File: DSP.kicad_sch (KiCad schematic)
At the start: 19 parts, among them J2 Conn_01x04, J4 Conn_01x04, J5 Conn_01x04, U4 STM32F103C6Tx, Y1 16MHz

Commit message: Added polygons
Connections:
- net V_USB is gone; now on net +3V3: J2.1 (Pin_1), J4.1 (Pin_1), J5.1 (Pin_1)
- net PB12 renamed RAM_nCS
- net PB13 renamed SD_nCS
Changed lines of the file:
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@@
-    )
-  )
-  (global_label "V_USB" (shape input) (at 214.63 97.79 90) (fields_autoplaced)
-    (effects (font (size 1 1)) (justify left))
-    (property "Intersheet References" "${INTERSHEET_REFS}" (id 0) (at 214.5675 91.271 90)
-      (effects (font (size 1 1)) (justify left) hide)
     )
   )
@@
     )
   )
-  (global_label "PB12" (shape input) (at 92.71 110.49 180) (fields_autoplaced)
-    (effects (font (size 1 1)) (justify right))
-    (property "Intersheet References" "${INTERSHEET_REFS}" (id 0) (at 86.9052 110.4275 0)
-      (effects (font (size 1 1)) (justify right) hide)
-    )
-  )
   (global_label "Tx" (shape input) (at 198.12 124.46 180) (fields_autoplaced)
     (effects (font (size 1 1)) (justify right))
@@
     )
   )
-  (global_label "PB13" (shape input) (at 92.71 113.03 180) (fields_autoplaced)
-    (effects (font (size 1 1)) (justify right))
-    (property "Intersheet References" "${INTERSHEET_REFS}" (id 0) (at 86.9052 112.9675 0)
+  (global_label "RAM_nCS" (shape input) (at 92.71 110.49 180) (fields_autoplaced)
+    (effects (font (size 1 1)) (justify right))
+    (property "Intersheet References" "${INTERSHEET_REFS}" (id 0) (at 84.191 110.5525 0)
       (effects (font (size 1 1)) (justify right) hide)
     )
@@
     )
   )
-  (global_label "V_USB" (shape input) (at 196.85 118.11 90) (fields_autoplaced)
-    (effects (font (size 1 1)) (justify left))
-    (property "Intersheet References" "${INTERSHEET_REFS}" (id 0) (at 196.7875 111.591 90)
-      (effects (font (size 1 1)) (justify left) hide)
-    )
-  )
   (global_label "PC15" (shape input) (at 92.71 74.93 180) (fields_autoplaced)
     (effects (font (size 1 1)) (justify right))
@@
     )
   )
-  (global_label "V_USB" (shape input) (at 186.69 97.79 90) (fields_autoplaced)
-    (effects (font (size 1 1)) (justify left))
-    (property "Intersheet References" "${INTERSHEET_REFS}" (id 0) (at 186.6275 91.271 90)
-      (effects (font (size 1 1)) (justify left) hide)
-    )
-  )
   (global_label "Tx" (shape input) (at 125.73 102.87 0) (fields_autoplaced)
     (effects (font (size 1 1)) (justify left))
@@
     (effects (font (size 1 1)) (justify right))
     (property "Intersheet References" "${INTERSHEET_REFS}" (id 0) (at 86.9052 115.5075 0)
+      (effects (font (size 1 1)) (justify right) hide)
+    )
+  )
+  (global_label "SD_nCS" (shape input) (at 92.71 113.03 180) (fields_autoplaced)
+    (effects (font (size 1 1)) (justify right))
+    (property "Intersheet References" "${INTERSHEET_REFS}" (id 0) (at 85.2386 112.9675 0)
       (effects (font (size 1 1)) (justify right) hide)
     )
@@
     (pin "1")
   )
+  (symbol (lib_id "power:+3.3V") (at 214.63 97.79 0) (unit 1)
+    (in_bom yes) (on_board yes) (fields_autoplaced)
+    (property "Reference" "#PWR?" (id 0) (at 214.63 101.6 0)
+      (effects (font (size 1.27 1.27)) hide)
+    )
+    (property "Value" "+3.3V" (id 1) (at 214.63 92.71 0))
+    (property "Footprint" "" (id 2) (at 214.63 97.79 0)
+      (effects (font (size 1.27 1.27)) hide)
+    )
+    (property "Datasheet" "" (id 3) (at 214.63 97.79 0)
+      (effects (font (size 1.27 1.27)) hide)
+    )
+    (pin "1")
+  )
   (symbol (lib_id "Device:C_Small") (at 142.24 52.07 0) (unit 1)
     (in_bom yes) (on_board yes)
@@
     (pin "1")
     (pin "2")
+  )
+  (symbol (lib_id "power:+3.3V") (at 186.69 97.79 0) (unit 1)
+    (in_bom yes) (on_board yes) (fields_autoplaced)
+    (property "Reference" "#PWR?" (id 0) (at 186.69 101.6 0)
+      (effects (font (size 1.27 1.27)) hide)
+    )
+    (property "Value" "+3.3V" (id 1) (at 186.69 92.71 0))
+    (property "Footprint" "" (id 2) (at 186.69 97.79 0)
+      (effects (font (size 1.27 1.27)) hide)
+    )
+    (property "Datasheet" "" (id 3) (at 186.69 97.79 0)
+      (effects (font (size 1.27 1.27)) hide)
+    )
+    (pin "1")
   )
   (symbol (lib_id "power:GND") (at 86.36 172.72 0) (unit 1)
@@
     (pin "9")
   )
+  (symbol (lib_id "power:+3.3V") (at 196.85 118.11 0) (unit 1)
+    (in_bom yes) (on_board yes) (fields_autoplaced)
+    (property "Reference" "#PWR?" (id 0) (at 196.85 121.92 0)
+      (effects (font (size 1.27 1.27)) hide)
+    )
+    (property "Value" "+3.3V" (id 1) (at 196.85 113.03 0))
+    (property "Footprint" "" (id 2) (at 196.85 118.11 0)
+      (effects (font (size 1.27 1.27)) hide)
+    )
+    (property "Datasheet" "" (id 3) (at 196.85 118.11 0)
+      (effects (font (size 1.27 1.27)) hide)
+    )
+    (pin "1")
+  )
   (symbol (lib_id "power:GND") (at 78.74 143.51 0) (unit 1)

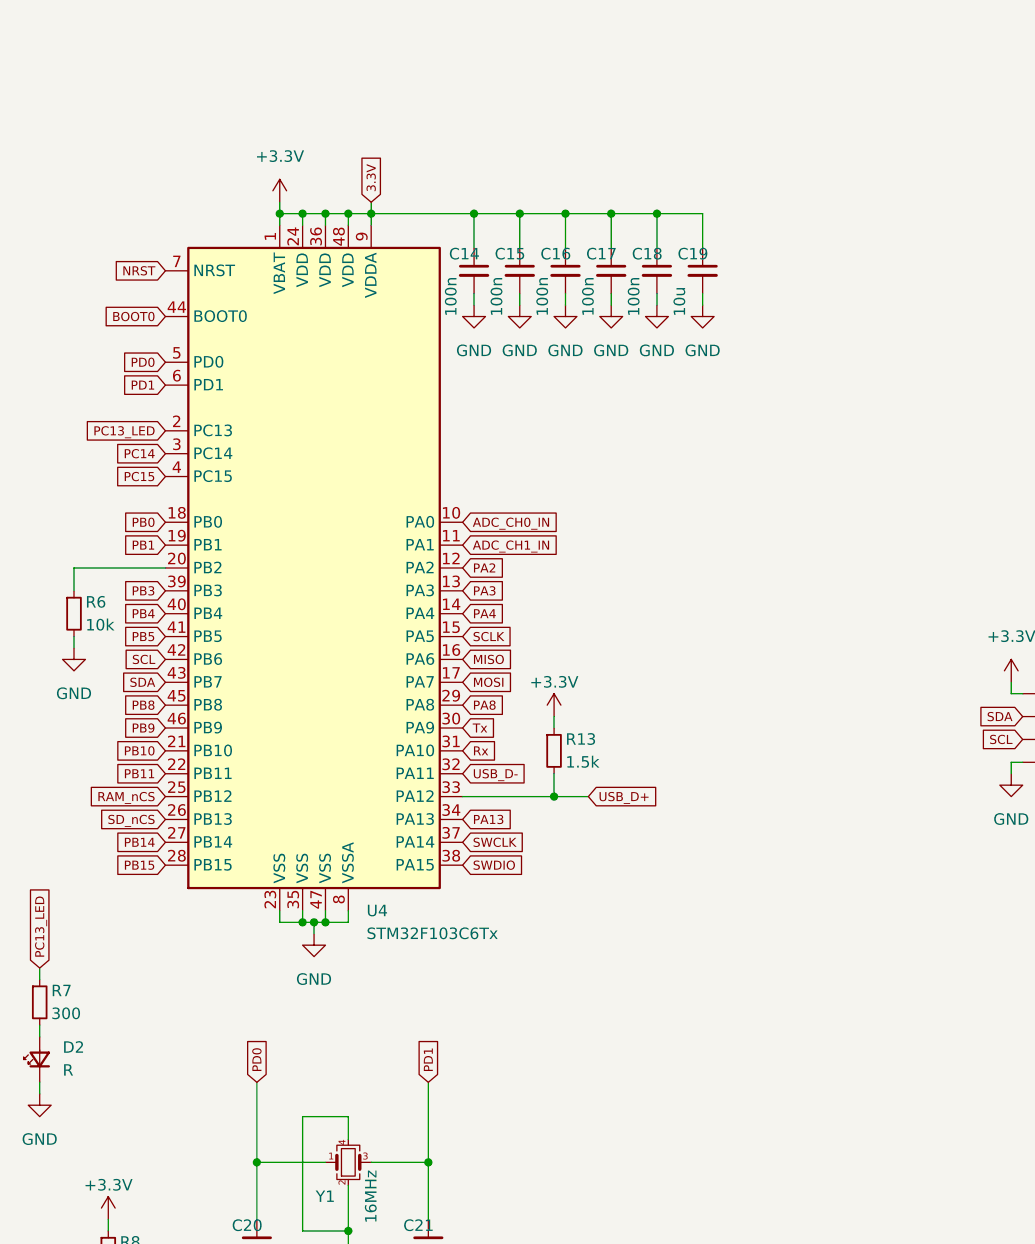
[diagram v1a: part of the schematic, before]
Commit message: had to change mcu since the stm32f103 does not have an FPU -> too slow for DSP applications
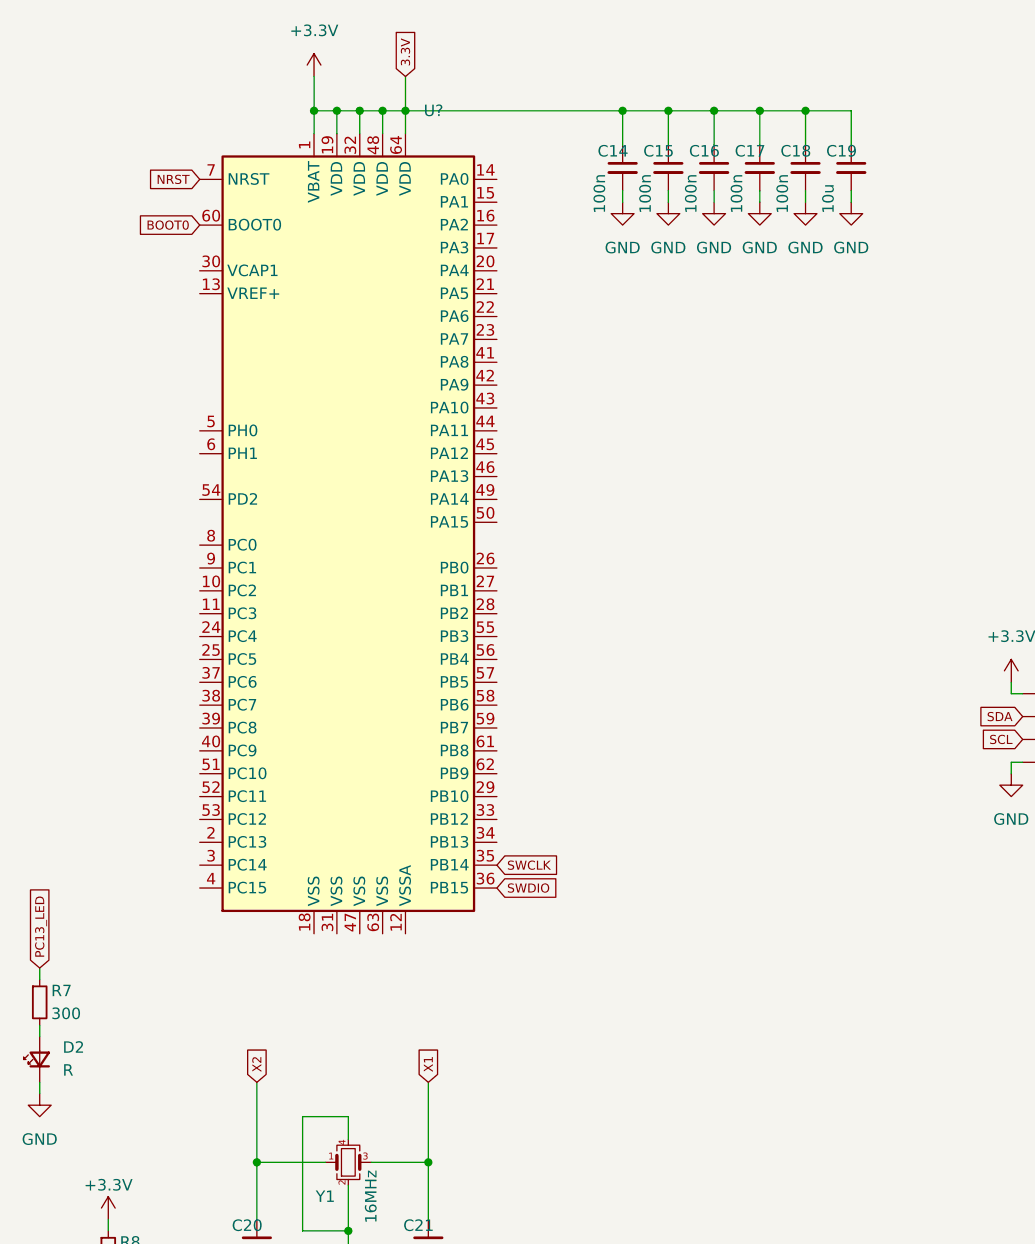
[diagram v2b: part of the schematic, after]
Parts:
- removed R13: 1.5k, Resistor_SMD:R_0603_1608Metric_Pad0.98x0.95mm_HandSolder, symbol Device:R_Small
- removed R6: 10k, Resistor_SMD:R_0603_1608Metric_Pad0.98x0.95mm_HandSolder, symbol Device:R_Small
- removed U4: STM32F103C6Tx, Package_QFP:LQFP-48_7x7mm_P0.5mm, symbol MCU_ST_STM32F1:STM32F103C6Tx
- added U?: (no value), symbol MCU_ST_STM32F4:STM32F401RBTx
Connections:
- net +3V3: now also U?.1 (VBAT), U?.19 (VDD), U?.32 (VDD), U?.48 (VDD), U?.64 (VDD)
- net BOOT0: now also U?.60 (BOOT0)
- net NRST: now also U?.7 (NRST)
- net SWCLK: now also U?.35 (PB14)
- net SWDIO: now also U?.36 (PB15)
- net PD0 renamed X2
- net PD1 renamed X1
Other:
- moved on the sheet: C14, C15, C16, C17, C18, C19

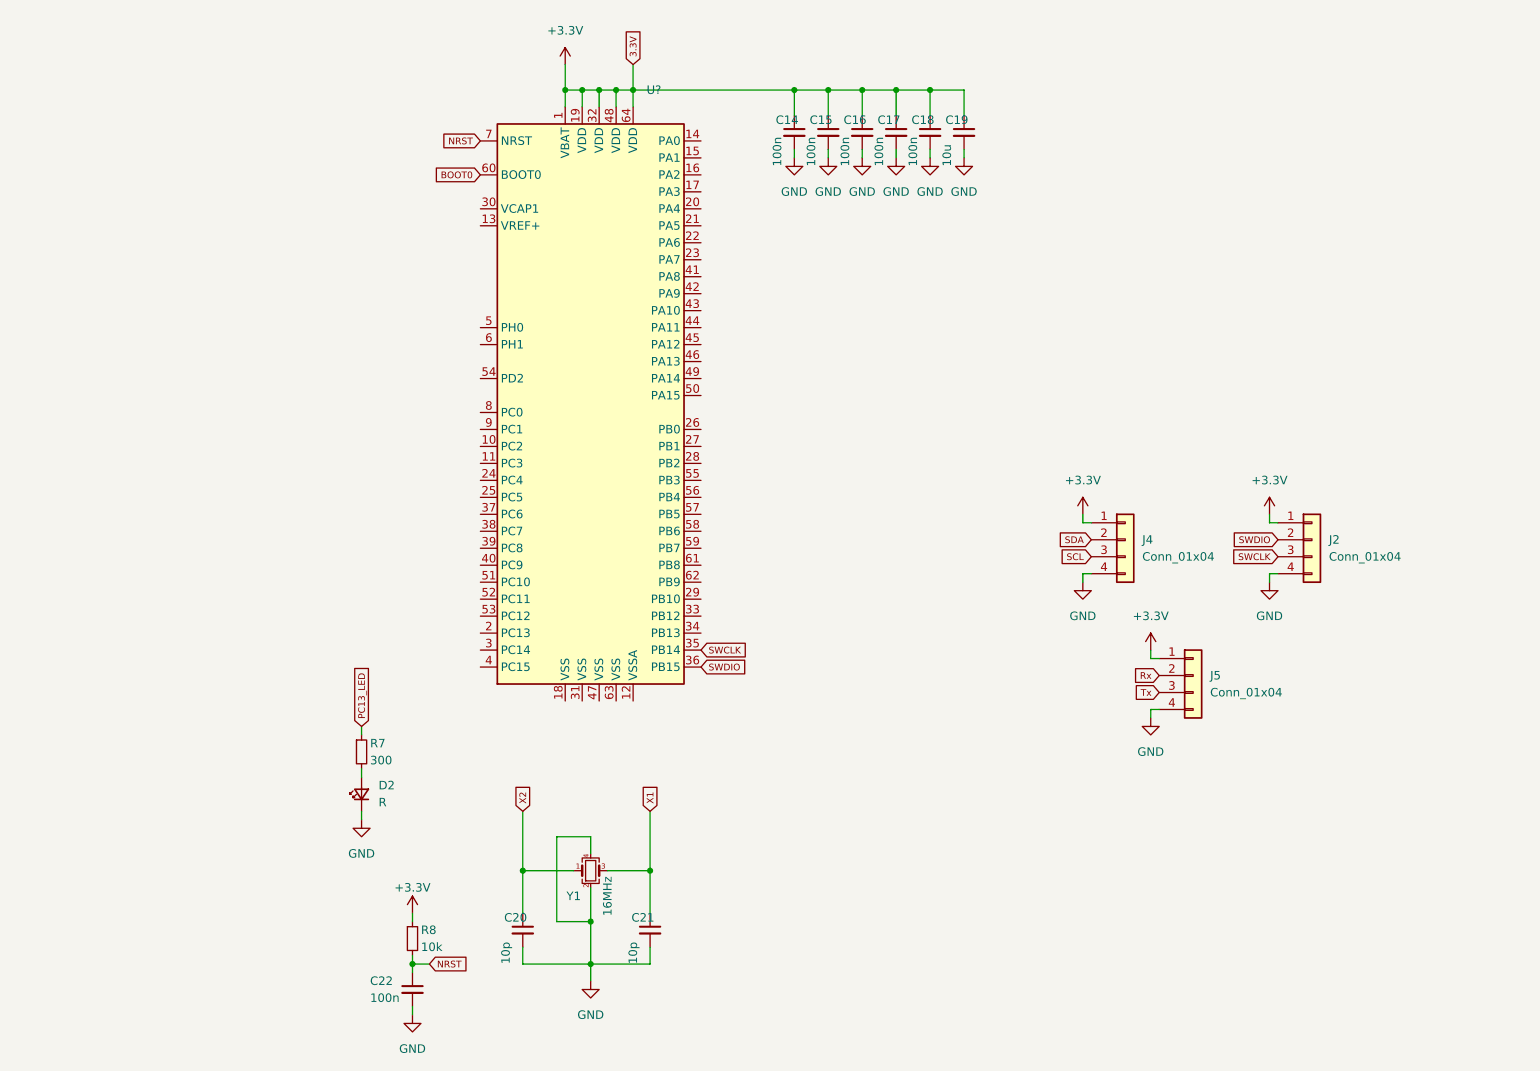
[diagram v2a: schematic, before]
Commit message: completed schematic and layout with new mcu, also added an SPI connector
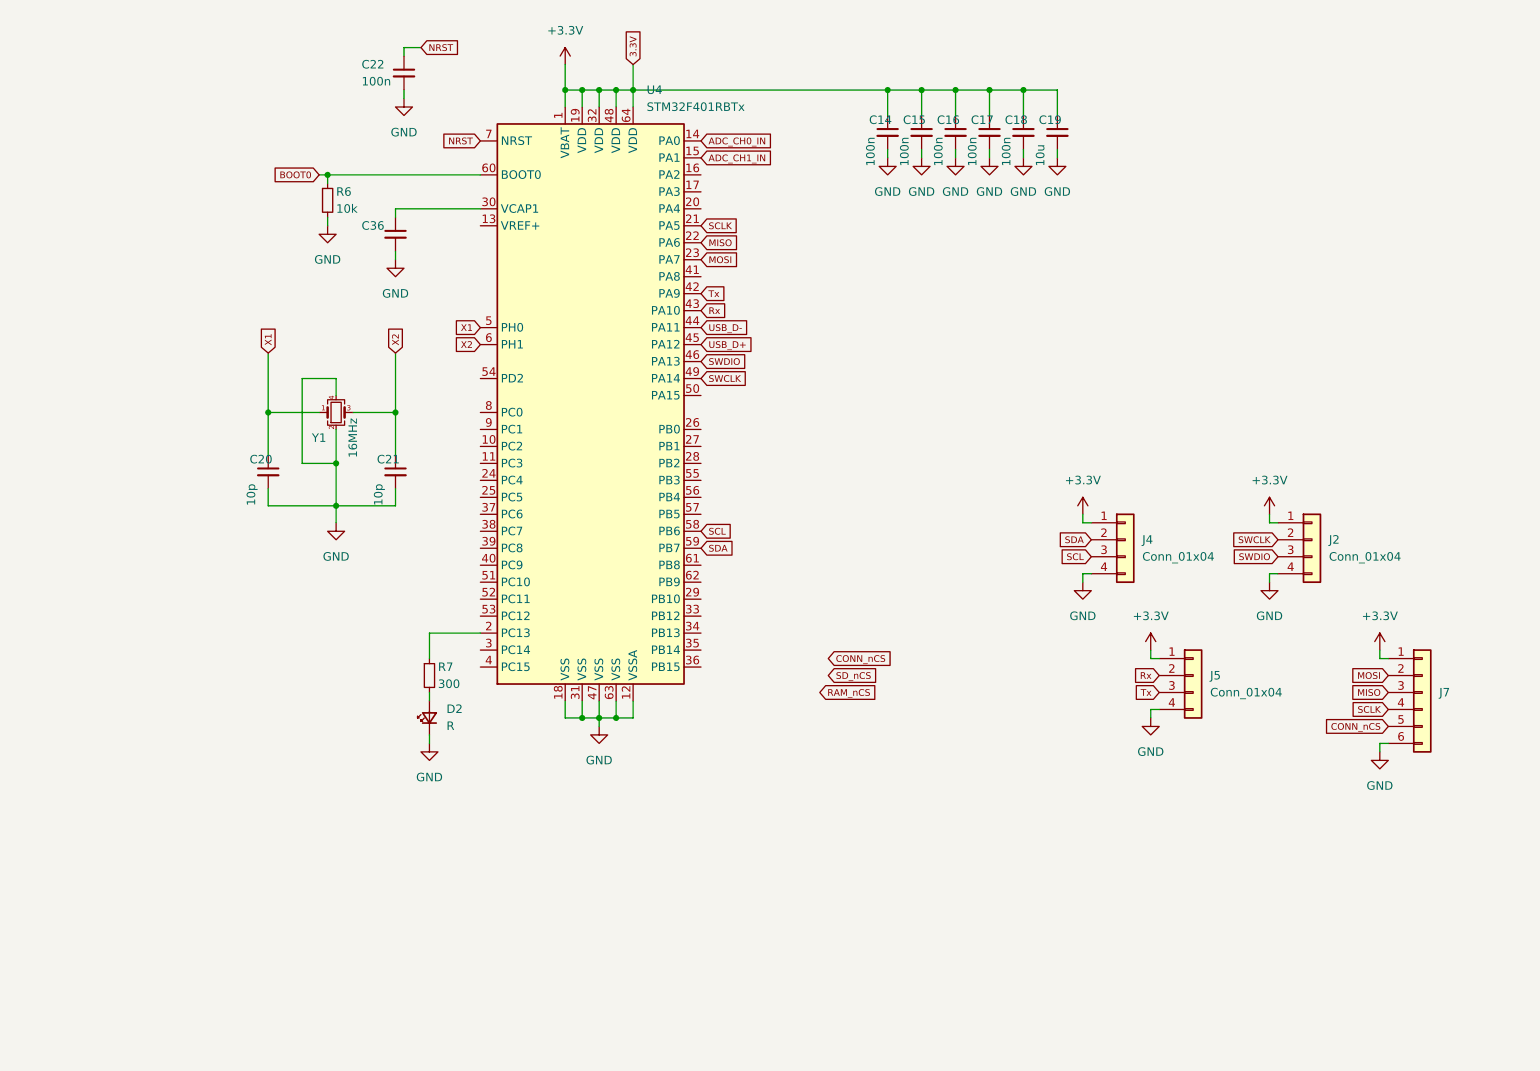
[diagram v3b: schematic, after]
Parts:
- removed R8: 10k, Resistor_SMD:R_0603_1608Metric_Pad0.98x0.95mm_HandSolder, symbol Device:R_Small
- added C36: (no value), symbol Device:C_Small
- added J7: (no value), symbol Connector_Generic:Conn_01x06
- added R6: 10k, Resistor_SMD:R_0603_1608Metric_Pad0.98x0.95mm_HandSolder, symbol Device:R_Small
- U4: renamed from U?; value (none) -> STM32F401RBTx; footprint (none) -> Package_QFP:LQFP-64_10x10mm_P0.5mm
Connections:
- net PC13_LED is gone; now on an unnamed net: R7.1
- net +3V3: now also J7.1 (Pin_1)
- net BOOT0: now also R6.1
- net GND: now also U4.12 (VSSA), U4.18 (VSS), U4.31 (VSS), U4.47 (VSS), U4.63 (VSS), C36.2, J7.6 (Pin_6), R6.2
- net Rx: now also U4.43 (PA10)
- net SCL: now also U4.58 (PB6)
- net SDA: now also U4.59 (PB7)
- net SWCLK: now also J2.2 (Pin_2), U4.49 (PA14); no longer J2.3 (Pin_3), U4.35 (PB14)
- net SWDIO: now also J2.3 (Pin_3), U4.46 (PA13); no longer J2.2 (Pin_2), U4.36 (PB15)
- net Tx: now also U4.42 (PA9)
- net X1: now also C20.1, U4.5 (PH0), Y1.1; no longer C21.1, Y1.3
- net X2: now also C21.1, U4.6 (PH1), Y1.3; no longer C20.1, Y1.1
- net ADC_CH0_IN: now reaches U4.14 (PA0)
- net ADC_CH1_IN: now reaches U4.15 (PA1)
- net SCLK: now reaches U4.21 (PA5)
- net SCLK: now also J7.4 (Pin_4)
- net MISO: now reaches U4.22 (PA6)
- net MISO: now also J7.3 (Pin_3)
- net MOSI: now reaches U4.23 (PA7)
- net MOSI: now also J7.2 (Pin_2)
- net at U4.30 (VCAP1): now also C36.1
- net USB_D-: now reaches U4.44 (PA11)
- net USB_D+: now reaches U4.45 (PA12)
- new net CONN_nCS: J7.5 (Pin_5)
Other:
- moved on the sheet: C14, C15, C16, C17, C18, C19, C20, C21, C22, D2, R7, Y1

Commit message: forgot the cs pins
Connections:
- net CONN_nCS: now also U4.24 (PC4)
- net RAM_nCS: now also U4.25 (PC5)
- net SD_nCS: now also U4.26 (PB0)
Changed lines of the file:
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@@
     )
   )
-  (global_label "RAM_nCS" (shape input) (at 147.32 124.46 0) (fields_autoplaced)
-    (effects (font (size 1 1)) (justify left))
-    (property "Intersheet References" "${INTERSHEET_REFS}" (id 0) (at 155.839 124.3975 0)
-      (effects (font (size 1 1)) (justify left) hide)
+  (global_label "RAM_nCS" (shape input) (at 96.52 95.25 180) (fields_autoplaced)
+    (effects (font (size 1 1)) (justify right))
+    (property "Intersheet References" "${INTERSHEET_REFS}" (id 0) (at 88.001 95.3125 0)
+      (effects (font (size 1 1)) (justify right) hide)
     )
   )
@@
     )
   )
-  (global_label "CONN_nCS" (shape input) (at 148.59 119.38 0) (fields_autoplaced)
-    (effects (font (size 1 1)) (justify left))
-    (property "Intersheet References" "${INTERSHEET_REFS}" (id 0) (at 158.2519 119.3175 0)
-      (effects (font (size 1 1)) (justify left) hide)
+  (global_label "CONN_nCS" (shape input) (at 96.52 92.71 180) (fields_autoplaced)
+    (effects (font (size 1 1)) (justify right))
+    (property "Intersheet References" "${INTERSHEET_REFS}" (id 0) (at 86.8581 92.7725 0)
+      (effects (font (size 1 1)) (justify right) hide)
     )
   )
@@
     )
   )
-  (global_label "SD_nCS" (shape input) (at 148.59 121.92 0) (fields_autoplaced)
+  (global_label "SD_nCS" (shape input) (at 129.54 85.09 0) (fields_autoplaced)
     (effects (font (size 1 1)) (justify left))
-    (property "Intersheet References" "${INTERSHEET_REFS}" (id 0) (at 156.0614 121.9825 0)
+    (property "Intersheet References" "${INTERSHEET_REFS}" (id 0) (at 137.0114 85.1525 0)
       (effects (font (size 1 1)) (justify left) hide)
     )

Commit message: added more silkscreen lables
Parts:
- C36: value (none) -> 10u; footprint (none) -> Capacitor_SMD:C_0603_1608Metric_Pad1.08x0.95mm_HandSolder
- J7: value (none) -> Conn_01x06; footprint (none) -> Connector_PinHeader_2.54mm:PinHeader_1x06_P2.54mm_Vertical
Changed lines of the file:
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@@
       (effects (font (size 1.27 1.27)) (justify left))
     )
-    (property "Value" "" (id 1) (at 78.74 57.15 0)
-      (effects (font (size 1.27 1.27)) (justify left))
-    )
-    (property "Footprint" "" (id 2) (at 83.82 55.88 0)
+    (property "Value" "10u" (id 1) (at 78.74 57.15 0)
+      (effects (font (size 1.27 1.27)) (justify left))
+    )
+    (property "Footprint" "Capacitor_SMD:C_0603_1608Metric_Pad1.08x0.95mm_HandSolder" (id 2) (at 83.82 55.88 0)
       (effects (font (size 1.27 1.27)) hide)
     )
@@
       (effects (font (size 1.27 1.27)) (justify left))
     )
-    (property "Value" "" (id 1) (at 240.03 126.9999 0)
-      (effects (font (size 1.27 1.27)) (justify left))
-    )
-    (property "Footprint" "" (id 2) (at 237.49 124.46 0)
-      (effects (font (size 1.27 1.27)) hide)
-    )
+    (property "Value" "Conn_01x06" (id 1) (at 240.03 126.9999 0)
+      (effects (font (size 1.27 1.27)) (justify left))
+    )
+    (property "Footprint" "Connector_PinHeader_2.54mm:PinHeader_1x06_P2.54mm_Vertical" (id 2) (at 237.49 124.46 0)
+      (effects (font (size 1.27 1.27)) hide)
+    )
